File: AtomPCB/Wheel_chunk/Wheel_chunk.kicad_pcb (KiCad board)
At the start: 2 copper layers, 9 parts, among them J1 DF40HC_4.0_-40DS-0.4V_70_, J2 Conn_01x04_Pin, J3 Conn_01x04_Pin, J4 Conn_01x04_Pin, J5 Conn_01x04_Pin, U1 ATtiny416-M, U3 DRV8834RGER, U4 DRV8834RGER, U6 MPM3610AGQV-P

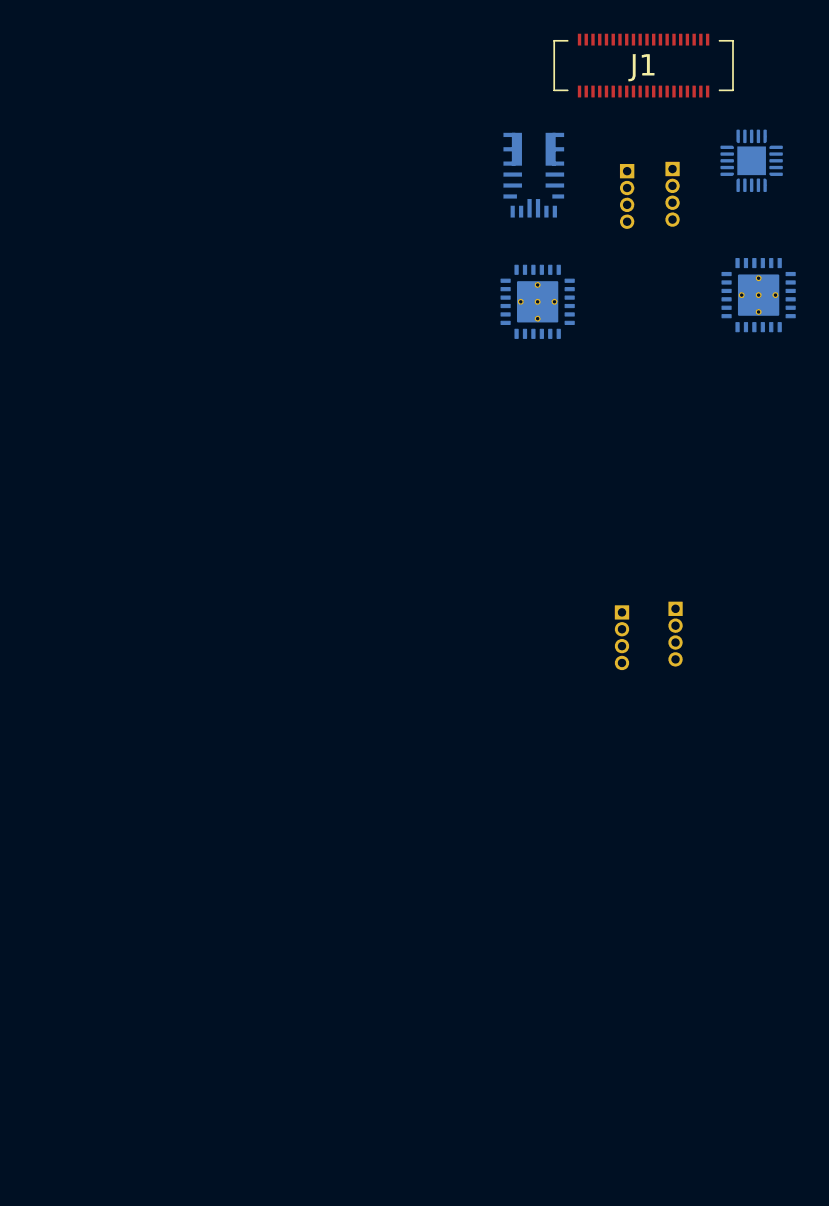
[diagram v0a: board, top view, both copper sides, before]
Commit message: adding core pcb templates. Finished rev 0.1 of wheel chunk pcb
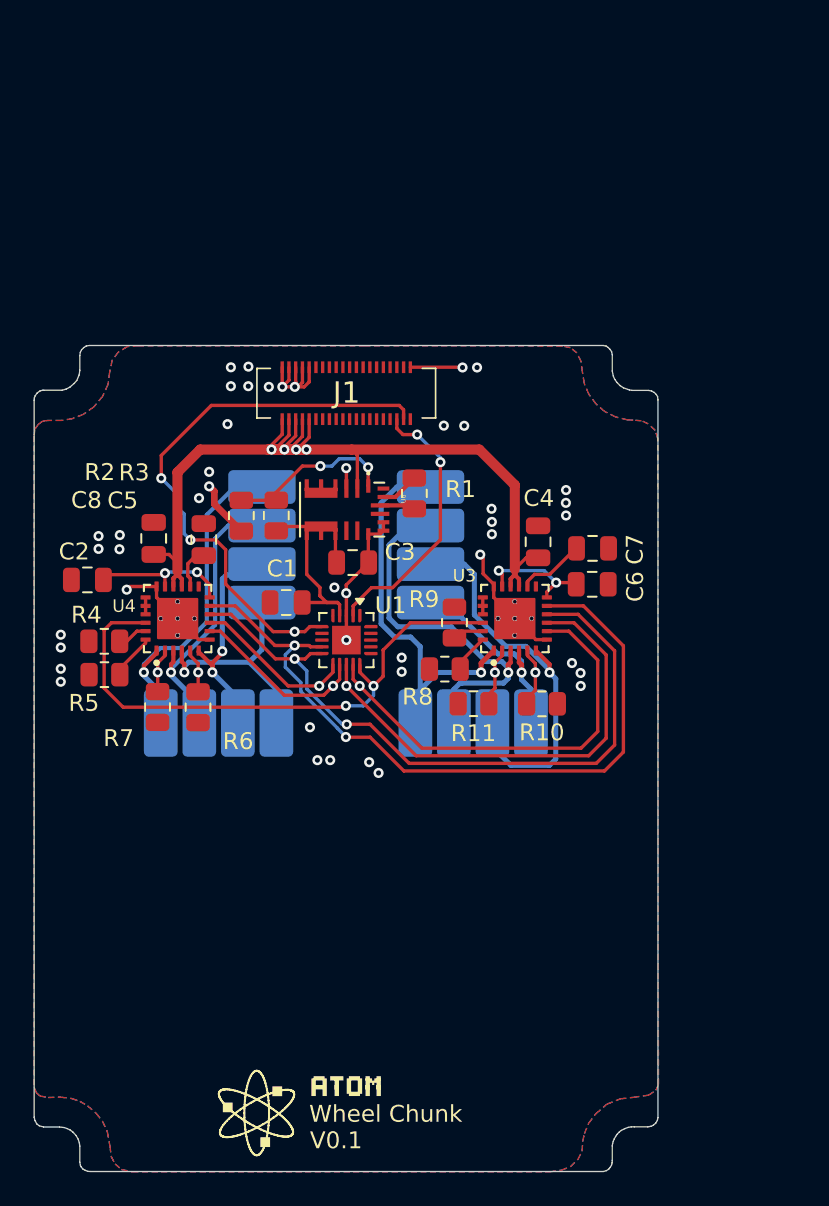
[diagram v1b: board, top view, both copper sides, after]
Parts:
- added C1: 22uf, Capacitor_SMD:C_0805_2012Metric, F.Cu at (123.4, 114.0)
- added C2: 2.2uf, Capacitor_SMD:C_0805_2012Metric, F.Cu at (111.7, 112.7)
- added C3: 22uF, Capacitor_SMD:C_0805_2012Metric, F.Cu at (127.4, 111.7)
- added C4: 10uf, Capacitor_SMD:C_0805_2012Metric, F.Cu at (138.4, 110.5)
- added C5: 10uf, Capacitor_SMD:C_0805_2012Metric, F.Cu at (115.6, 110.2)
- added C6: 2.2uf, Capacitor_SMD:C_0805_2012Metric, F.Cu at (141.6, 113.0)
- added C7: 0.01uf, Capacitor_SMD:C_0805_2012Metric, F.Cu at (141.6, 110.8)
- added C8: 0.01uf, Capacitor_SMD:C_0805_2012Metric, F.Cu at (118.5, 110.3)
- added R1: 75K, Resistor_SMD:R_0805_2012Metric, F.Cu at (131.0, 107.6)
- added R10: 50k, Resistor_SMD:R_0805_2012Metric, F.Cu at (138.6, 120.1)
- added R11: 50k, Resistor_SMD:R_0805_2012Metric, F.Cu at (134.6, 120.0)
- added R2: 24K, Resistor_SMD:R_0805_2012Metric, F.Cu at (120.8, 108.9)
- added R3: 75K, Resistor_SMD:R_0805_2012Metric, F.Cu at (122.8, 108.9)
- added R4: 50k, Resistor_SMD:R_0805_2012Metric, F.Cu at (112.7, 116.3)
- added R5: 50k, Resistor_SMD:R_0805_2012Metric, F.Cu at (112.7, 118.3)
- added R6: 50k, Resistor_SMD:R_0805_2012Metric, F.Cu at (118.2, 120.3)
- added R7: 50k, Resistor_SMD:R_0805_2012Metric, F.Cu at (115.8, 120.2)
- added R8: 50k, Resistor_SMD:R_0805_2012Metric, F.Cu at (132.8, 118.0)
- added R9: 50k, Resistor_SMD:R_0805_2012Metric, F.Cu at (133.4, 115.2)
- J2, J3, J4, J5: footprint Connector_PinHeader_1.00mm:PinHeader_1x04_P1.00mm_Vertical -> Wire_flat_pads:PAD_1x4_4.0x2.0
- U1, U3, U4, U6: moved to F.Cu
- moved J5 44.7 mm to (116.0, 121.2), turned to -90 degrees
- moved U4 39.4 mm to (117.0, 115.0), turned to 90 degrees
- moved U1 37.2 mm to (127.0, 116.3), turned to -90 degrees
- moved J1 26.2 mm to (127.0, 101.6)
- moved J4 25.6 mm to (122.0, 107.2)
- moved U6 23.1 mm to (126.8, 108.5), turned to -90 degrees
- moved J2 22.1 mm to (132.0, 107.2)
- moved U3 18.8 mm to (137.0, 115.0), turned to 90 degrees
- moved J3 13.9 mm to (131.1, 121.2), turned to -90 degrees
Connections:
- J1 pad 12: unconnected-(J1-Pad12) -> /PWM1
- J1 pad 14: unconnected-(J1-Pad14) -> /PWM2
- J1 pad 16: unconnected-(J1-Pad16) -> /PWM3
- J1 pad 18: unconnected-(J1-Pad18) -> /PWM4
- J1 pad 20: unconnected-(J1-Pad20) -> /PWM5
- J1 pad 22: unconnected-(J1-Pad22) -> /PWM6
- J1 pad 23: unconnected-(J1-Pad23) -> /ADC
- J1 pad 24: unconnected-(J1-Pad24) -> /PWM7
- J1 pad 25: unconnected-(J1-Pad25) -> /DCA
- J1 pad 26: unconnected-(J1-Pad26) -> /PWM8
- J1 pad 31: unconnected-(J1-Pad31) -> /EN1
- J1 pad 33: unconnected-(J1-Pad33) -> /EN2
- U3 pad 12: unconnected-(U3-CONFIG-Pad12) -> /CFG1
- U3 pad 14: unconnected-(U3-VCP-Pad14) -> Net-(U3-VCP)
- U3 pad 17: unconnected-(U3-VINT-Pad17) -> /CFG1
- U3 pad 19: unconnected-(U3-AVREF-Pad19) -> /REF1
- U3 pad 2: unconnected-(U3-AISEN-Pad2) -> Net-(U3-AISEN)
- U3 pad 20: unconnected-(U3-BVREF-Pad20) -> /REF1
- U3 pad 21: unconnected-(U3-VREFO-Pad21) -> /REF1
- U3 pad 23: unconnected-(U3-BDECAY-Pad23) -> Net-(U3-BDECAY)
- U3 pad 24: unconnected-(U3-ADECAY-Pad24) -> Net-(U3-ADECAY)
- U3 pad 5: unconnected-(U3-BISEN-Pad5) -> Net-(U3-BISEN)
- U3 pad 7: unconnected-(U3-NENBL/AENBL-Pad7) -> GND
- U4 pad 12: unconnected-(U4-CONFIG-Pad12) -> /CFG2
- U4 pad 14: unconnected-(U4-VCP-Pad14) -> Net-(U4-VCP)
- U4 pad 17: unconnected-(U4-VINT-Pad17) -> /CFG2
- U4 pad 19: unconnected-(U4-AVREF-Pad19) -> /REF2
- U4 pad 2: unconnected-(U4-AISEN-Pad2) -> Net-(U4-AISEN)
- U4 pad 20: unconnected-(U4-BVREF-Pad20) -> /REF2
- U4 pad 21: unconnected-(U4-VREFO-Pad21) -> /REF2
- U4 pad 23: unconnected-(U4-BDECAY-Pad23) -> Net-(U4-BDECAY)
- U4 pad 24: unconnected-(U4-ADECAY-Pad24) -> Net-(U4-ADECAY)
- U4 pad 5: unconnected-(U4-BISEN-Pad5) -> Net-(U4-BISEN)
- U4 pad 7: unconnected-(U4-NENBL/AENBL-Pad7) -> GND
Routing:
- net VBATT: track 0.00 -> 57.0 mm, vias 0 -> 4
- net /MICRO_STEP_SEL_2: track 0.00 -> 44.7 mm, vias 0 -> 2
- net /MICRO_STEP_SEL_1: track 0.00 -> 41.0 mm, vias 0 -> 2
- net GND: track 0.00 -> 37.5 mm, vias 0 -> 45
- net /EN: track 0.00 -> 34.0 mm, vias 0 -> 2
- net /SCL1: track 0.00 -> 33.4 mm, vias 0 -> 3
- net /DIR_1: track 0.00 -> 28.1 mm, vias 0 -> 1
- net /M1A+: track 0.00 -> 25.8 mm, vias 0 -> 1
- net /STEP_1: track 0.00 -> 25.5 mm, vias 0 -> 1
- net /M1B+: track 0.00 -> 23.9 mm, vias 0 -> 1
- net /M1A-: track 0.00 -> 23.0 mm, vias 0 -> 1
- net /M3A+: track 0.00 -> 20.6 mm, vias 0 -> 1
- net /M3A-: track 0.00 -> 17.2 mm, vias 0 -> 1
- net /SDA1: track 0.00 -> 16.1 mm, vias 0 -> 2
- net /M3B-: track 0.00 -> 13.8 mm, vias 0 -> 1
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- added copper zone on B.Cu, net GND
- added copper zone on F.Cu, net GND
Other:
- board outline added: 37 x 49 mm
- board text added: "A+"
- board text added: "A-"
- board text added: "B+"
- board text added: "B-"
- board text added: "M1"
- board text added: "M2"
- board text added: "M3"
- board text added: "M4"
- board text added: "V0.1"
- board text added: "Wheel Chunk"
